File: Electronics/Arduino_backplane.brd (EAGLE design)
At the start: 100 x 80 mm, 40 parts, among them IC1 4013N, IC2 MCP4802, IC3 MCP4802, Q1 BF199, Q5 BF199, X1 M25-HD-20, X2 M25-HD-20

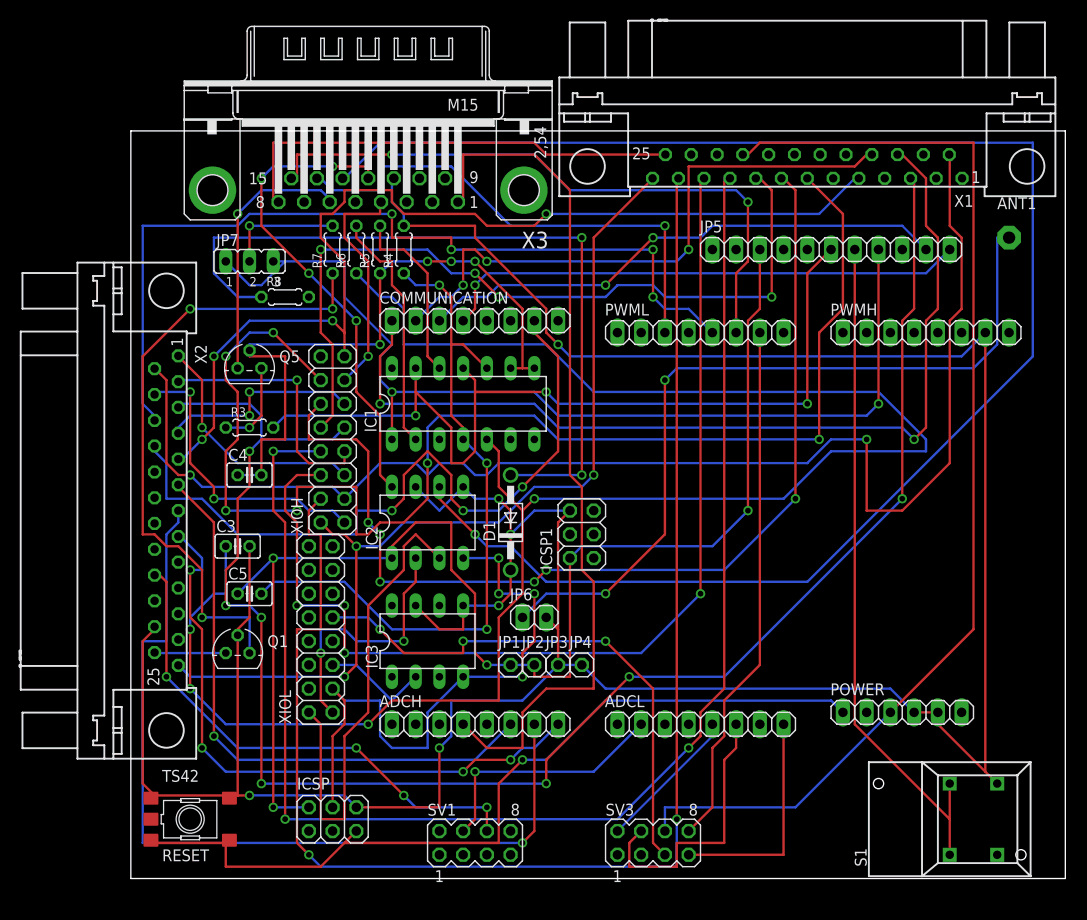
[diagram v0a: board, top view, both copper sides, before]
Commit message: Board layout improved, closer to Arduino pins. Signals renamed.
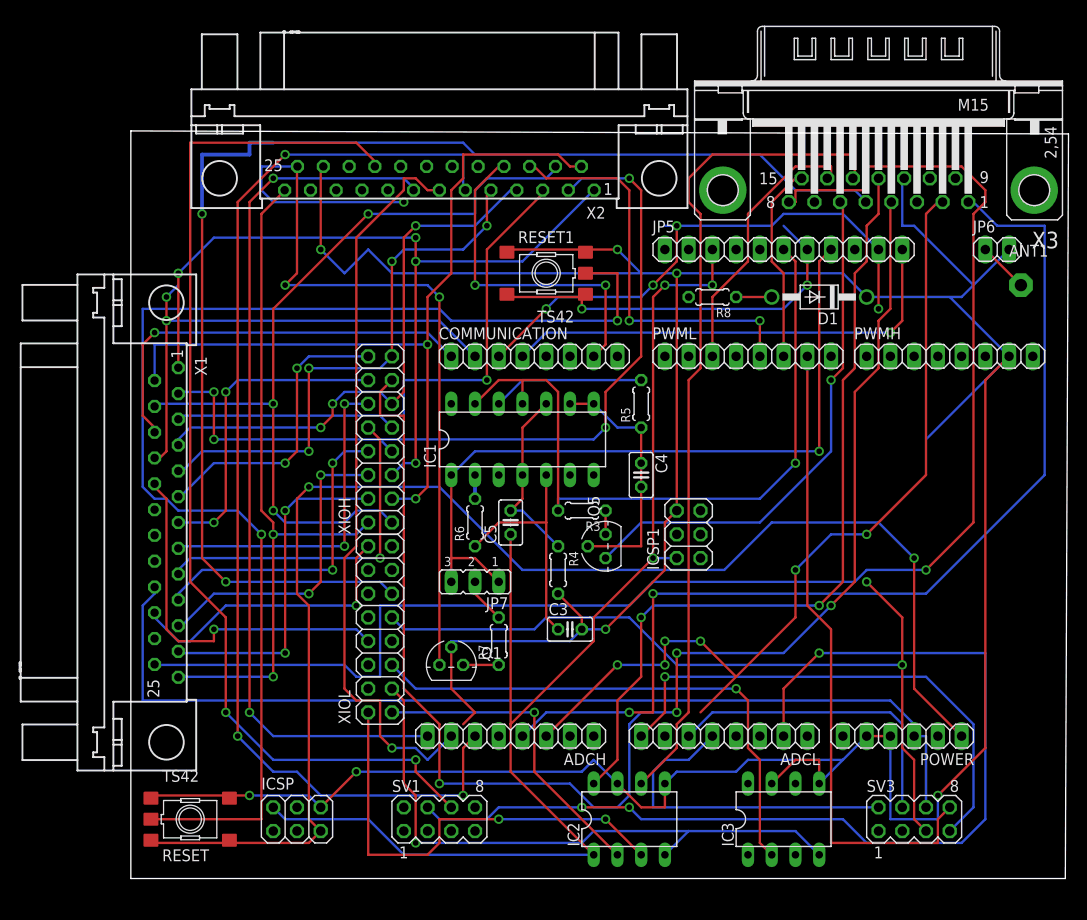
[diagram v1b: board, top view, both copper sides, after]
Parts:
- removed JP1, JP2, JP3, JP4: (no value), pinhead:1X01
- removed S1: 5501, switch:5501
- added RESET1: TS42, st-mod v1.4:TS42
- moved X1 78.5 mm to (3.81, 38.1), turned to 270 degrees
- moved JP6 63.3 mm to (92.7, 67.3)
- moved X3 54.6 mm to (80.0, 73.7)
- moved X2 46.0 mm to (33.0, 74.9), turned to 180 degrees
- moved R8 45.7 mm to (62.2, 62.2), turned to 180 degrees
- moved R7 45.5 mm to (39.4, 25.4)
- moved IC3 42.6 mm to (69.8, 6.35)
- moved Q5 42.6 mm to (50.8, 35.6), turned to 90 degrees
- moved JP7 41.9 mm to (36.8, 31.8), turned to 180 degrees
- moved C4 41.9 mm to (54.6, 43.2), turned to 270 degrees
- moved D1 40.9 mm to (73.7, 62.2), turned to 180 degrees
- moved IC2 38.4 mm to (53.3, 6.35)
- moved R4 38.1 mm to (45.7, 33.0), turned to 270 degrees
- moved C3 36.7 mm to (47.0, 26.7)
- moved R3 36.7 mm to (48.3, 39.4), turned to 180 degrees
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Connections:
- net INT0 renamed D2INT0
- net INT1 renamed D3INT1
- net INT2 renamed D18INT2
- net INT3 renamed D19INT3
- net INT4 renamed D20INT4
- net INT5 renamed D21INT5
- net N$1 renamed D25
- net N$10 renamed DACC
- net N$12 renamed D48
- net N$15 renamed WLES
- net N$19 renamed FUEL
- net N$2 renamed D4
- net N$20 renamed WLX
- net N$23 renamed VCC
- net N$3 renamed DACA
- net N$4 renamed D5
- net N$5 renamed D52
- net N$6 renamed DACB
- net N$8 renamed 5V
- net N$9 renamed A7
- net PA0 renamed D22
- net PA1 renamed D23
- net PA2 renamed D24
- net PA4 renamed D26
- net PA5 renamed D27
- net PA6 renamed D28
- net PA7 renamed D29
- net PB0 renamed D53
- net PB4 renamed D10
- net PB5 renamed D11
- net PB6 renamed D12
- net PB7 renamed D13
- net PC0 renamed D37
- net PC1 renamed D36
- net PC2 renamed D35
- net PC3 renamed D34
- net PC4 renamed D33
- net PC5 renamed D32
- net PC6 renamed D31
- net PC7 renamed D30
- net PD7 renamed D38
- net PG0 renamed D41
- net PG1 renamed D40
- net PG2 renamed D39
- net PH5 renamed D8
- net PH6 renamed D9
- net PL0 renamed D49
- net PL2 renamed D47
- net PL3 renamed D46
- net PL4 renamed D45
- net PL5 renamed D44
- net PL7 renamed D42
- net RXD2 renamed D17RXD2
- net RXD3 renamed D15RXD3
- net TXD2 renamed D16TXD2
- net TXD3 renamed D14TXD3
- removed net N$13: X3.5
- removed net N$37: R8.2
- removed net PL6: XIOL.11
- new net D43: X3.5, XIOL.11
- new net D51: IC2.4, IC3.4, XIOL.3
- new net DACD: IC3.6
- net +5V: no longer JP1.1, JP2.1
- net 5-GND: now also RESET1.5
- net GND: now also RESET1.3, RESET1.4; no longer JP3.1, JP4.1, S1.NO
- net N$28: now also RESET1.1, RESET1.2; no longer S1.1A, S1.1B
- net PB2: no longer IC2.4, IC3.4, XIOL.3
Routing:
- net N$35: track 201.4 -> 25.7 mm, vias 4 -> 0
- net D43: track 0.00 -> 140.2 mm, vias 0 -> 2
- net 5-GND: track 0.00 -> 136.4 mm, vias 0 -> 2
- net D25: track 25.1 -> 153.8 mm, vias 1 -> 4
- net D30: track 154.5 -> 34.0 mm, vias 3 -> 2
- net D34: track 156.7 -> 36.3 mm
- net D29: track 181.1 -> 62.3 mm, vias 7 -> 1
- net FUEL: track 49.4 -> 161.5 mm, vias 0 -> 1
- net D24: track 143.3 -> 34.1 mm, vias 6 -> 2
- net A10: track 0.00 -> 95.5 mm, vias 0 -> 6
- net DACB: track 176.7 -> 89.5 mm, vias 1 -> 0
- net WLX: track 7.67 -> 91.8 mm, vias 0 -> 3
- net A1: track 26.8 -> 109.4 mm, vias 1 -> 3
- net N$26: track 85.3 -> 5.39 mm, vias 2 -> 0
- net D32: track 113.3 -> 34.2 mm, vias 4 -> 2
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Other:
- board size 100 x 80 mm -> 100.3 x 80 mm

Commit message: Moved components for better routing; corrected connection errors.
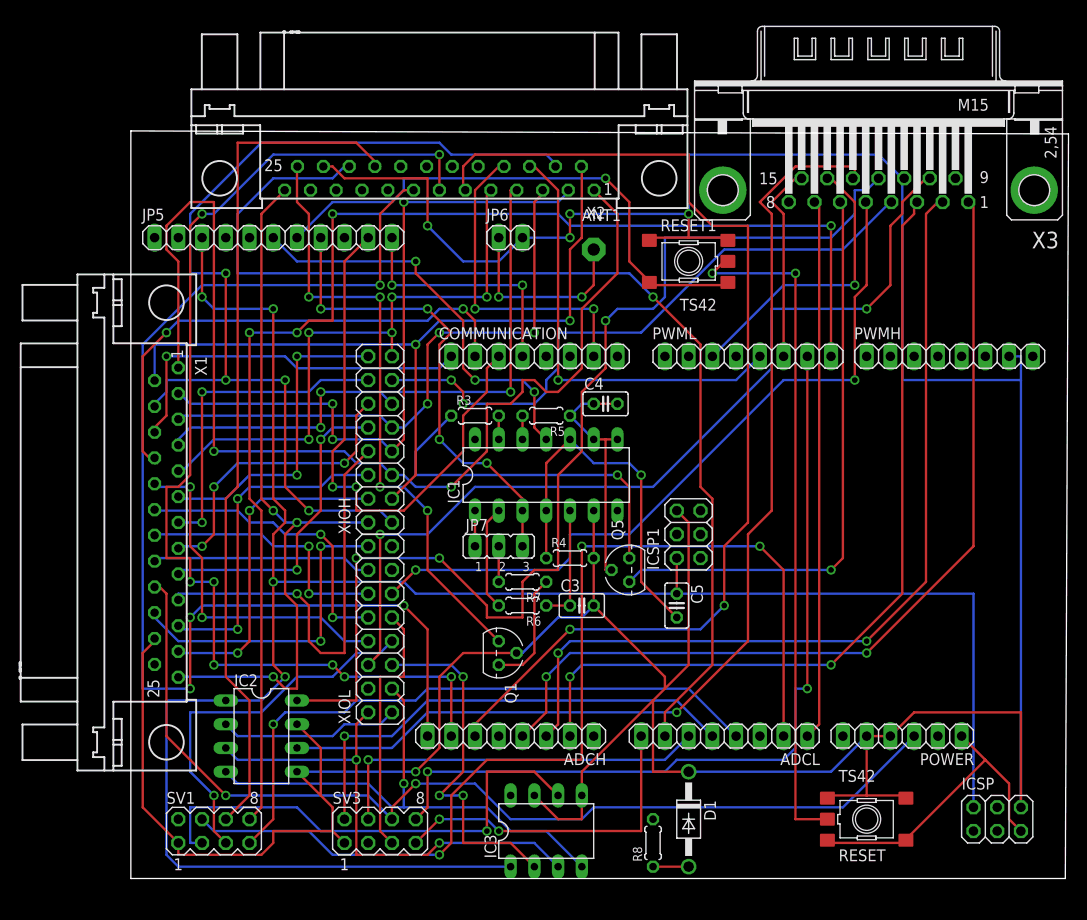
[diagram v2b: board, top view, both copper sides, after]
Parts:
- moved ICSP 74.9 mm to (92.7, 6.35)
- moved RESET 72.4 mm to (78.7, 6.35)
- moved R8 58.8 mm to (55.9, 3.81), turned to 90 degrees
- moved D1 57.6 mm to (59.7, 6.35), turned to 270 degrees
- moved SV3 57.2 mm to (26.7, 5.08)
- moved JP5 54.6 mm to (15.2, 68.6)
- moved JP6 52.1 mm to (40.6, 68.6)
- moved ANT1 45.9 mm to (49.5, 67.3)
- moved IC2 40.4 mm to (14.0, 15.2), turned to 270 degrees
- moved IC3 25.4 mm to (44.5, 5.08)
- moved SV1 24.2 mm to (8.89, 5.08)
- moved C5 19.9 mm to (58.4, 29.2), turned to 270 degrees
- moved R3 15.3 mm to (36.8, 49.5), turned to 0 degrees
- moved RESET1 15.3 mm to (59.7, 66.0)
- moved R6 10.2 mm to (41.9, 29.2), turned to 180 degrees
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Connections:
- net 5V renamed 5VBRK
- net A8 renamed N$2
- removed net A2: ADCL.3
- new net A6: ADCL.7, X2.23
- new net N$1: SV1.2
- new net N$3: XIOL.4
- new net N$4: IC1.1, JP7.1
- new net N$5: IC1.13, R3.2
- net +5V: now also IC3.1
- net A0: now also ADCL.1
- net A3: now also SV1.7
- net A9: now also ADCH.2
- net D40: now also X1.21
- net D42: now also X1.20
- net D44: now also X1.19
- net D47: now also SV1.5
- net D48: now also XIOL.6
- net D52: now also IC3.3
- net D7: now also SV1.8
- net DACD: now also SV1.3
- net GND: now also IC1.6, SV1.1, SV3.1, X1.24
- net N$25: no longer IC1.13, R3.2
- net N$30: now also IC1.3; no longer IC1.1, JP7.1
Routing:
- net FUEL: track 161.5 -> 0.00 mm, vias 1 -> 0
- net D7: track 0.00 -> 141.8 mm, vias 0 -> 4
- net A6: track 0.00 -> 117.6 mm, vias 0 -> 1
- net RESET: track 151.0 -> 34.0 mm, vias 2 -> 0
- net D48: track 0.00 -> 97.3 mm, vias 0 -> 2
- net A9: track 0.00 -> 88.3 mm, vias 0 -> 2
- net D25: track 153.8 -> 67.2 mm, vias 4 -> 2
- net +5V: track 139.6 -> 225.2 mm, vias 3 -> 4
- net A3: track 0.00 -> 67.0 mm, vias 0 -> 1
- net 5-GND: track 136.4 -> 73.3 mm
- net D43: track 140.2 -> 80.2 mm
- net D45: track 87.1 -> 27.7 mm, vias 2 -> 0
- net A0: track 0.00 -> 58.2 mm
- net DACD: track 0.00 -> 52.9 mm, vias 0 -> 1
- net A14: track 79.4 -> 119.8 mm, vias 1 -> 8
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
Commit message: Corrected some overlaps
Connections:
- removed net N$3: XIOL.4
- net D14TXD3: now also X2.18
- net D16TXD2: now also X2.20
- net D17RXD2: now also X2.19
- net D3INT1: now also X2.21
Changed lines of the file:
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@@
 <signal name="D3INT1">
 <contactref element="PWML" pad="4"/>
+<contactref element="X2" pad="21"/>
+<wire x1="28.8798" y1="76.2" x2="64.77" y2="55.88" width="0" layer="19" extent="1-1"/>
 </signal>
 <signal name="D2INT0">
@@
 <signal name="D17RXD2">
 <contactref element="COMMUNICATION" pad="5"/>
+<contactref element="X2" pad="19"/>
+<wire x1="44.45" y1="55.88" x2="34.3916" y2="76.2" width="0" layer="19" extent="1-1"/>
 </signal>
 <signal name="D15RXD3">
@@
 <signal name="D16TXD2">
 <contactref element="COMMUNICATION" pad="6"/>
+<contactref element="X2" pad="20"/>
+<wire x1="46.99" y1="55.88" x2="31.6484" y2="76.2" width="0" layer="19" extent="1-1"/>
 </signal>
 <signal name="D14TXD3">
 <contactref element="COMMUNICATION" pad="8"/>
+<contactref element="X2" pad="18"/>
+<wire x1="52.07" y1="55.88" x2="37.1602" y2="76.2" width="0" layer="19" extent="1-1"/>
 </signal>
 <signal name="D37">
@@
 <wire x1="27.94" y1="27.94" x2="29.21" y2="26.67" width="0.254" layer="1"/>
 </signal>
-<signal name="N$3">
-<contactref element="XIOL" pad="4"/>
-</signal>
 <signal name="FUEL">

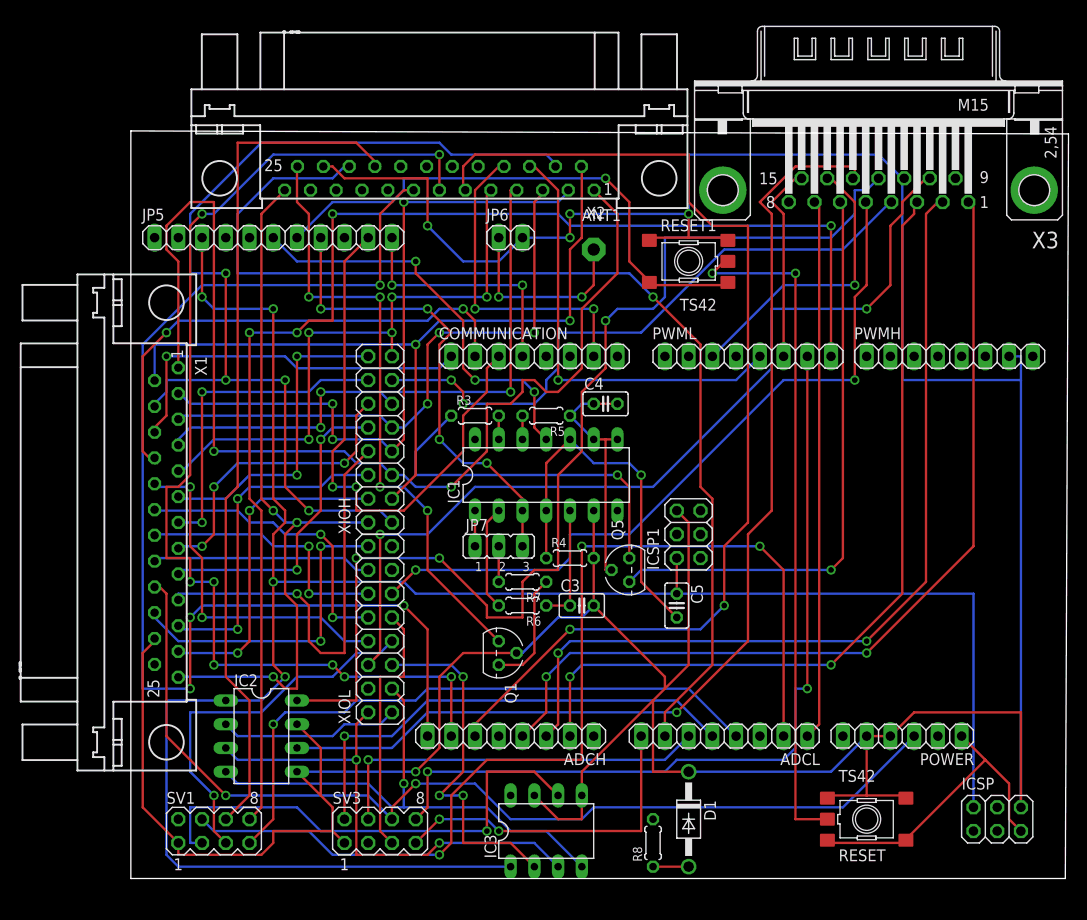
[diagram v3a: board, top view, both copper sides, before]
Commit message: Reduced warnings; 97% routed.
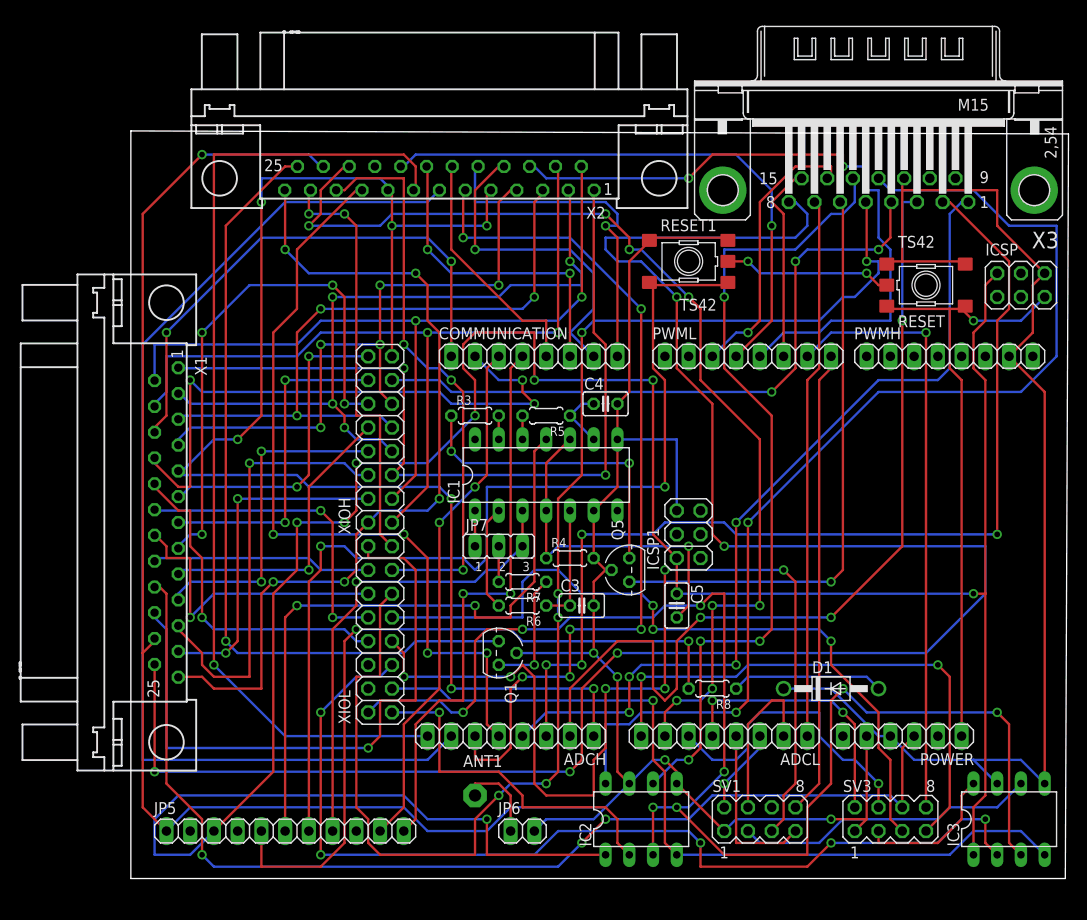
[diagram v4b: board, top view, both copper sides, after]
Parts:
- moved JP5 63.5 mm to (16.5, 5.08)
- moved JP6 63.5 mm to (41.9, 5.08)
- moved ANT1 59.8 mm to (36.8, 8.89)
- moved SV1 58.4 mm to (67.3, 6.35)
- moved RESET 57.5 mm to (85.1, 63.5)
- moved ICSP 57.2 mm to (95.2, 63.5)
- moved SV3 54.6 mm to (81.3, 6.35)
- moved IC3 49.5 mm to (94.0, 6.35)
- moved IC2 41.6 mm to (54.6, 6.35), turned to 0 degrees
- moved D1 20.7 mm to (74.9, 20.3), turned to 0 degrees
- moved R8 17.7 mm to (62.2, 20.3), turned to 180 degrees
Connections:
- removed net +3V3: POWER.2
- removed net AREF: PWMH.8
- removed net D10: PWMH.3
- removed net D11: PWMH.4
- removed net D12: PWMH.5
- removed net D13: PWMH.6
- removed net D8: PWMH.1
- removed net D9: PWMH.2
- removed net N$11: C4.1, C4.2, IC1.8, IC1.9, Q5.2, R5.1
- new net N$3: JP5.5, R8.2
- net A12: now also X2.10
- net D23: now also ADCH.1, X2.9
- net D39: now also X2.12
- net D41: now also X2.11
- net DACC: now also SV3.3
- net GND: now also C4.2, IC1.8, JP5.1, Q5.2
- net N$1: now also ADCL.3
- net N$2: now also C4.1, IC1.9, R5.1; no longer ADCH.1
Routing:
- net FUEL: track 0.00 -> 211.4 mm, vias 0 -> 5
- net D52: track 53.4 -> 150.7 mm, vias 2 -> 8
- net D48: track 97.3 -> 0.00 mm, vias 2 -> 0
- net A1: track 112.7 -> 17.6 mm, vias 3 -> 0
- net D7: track 141.8 -> 49.8 mm, vias 4 -> 0
- net 5VBRK: track 91.9 -> 0.00 mm
- net D23: track 64.7 -> 155.8 mm, vias 5 -> 7
- net A12: track 0.00 -> 84.6 mm, vias 0 -> 4
- net N$3: track 0.00 -> 78.3 mm, vias 0 -> 2
- net D47: track 40.3 -> 110.9 mm, vias 1 -> 6
- net D49: track 38.2 -> 106.6 mm, vias 3 -> 5
- net D43: track 80.2 -> 148.4 mm, vias 2 -> 6
- net D3INT1: track 0.00 -> 61.2 mm, vias 0 -> 1
- net D41: track 0.00 -> 61.1 mm, vias 0 -> 3
- net +5V: track 225.2 -> 284.2 mm, vias 4 -> 8
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
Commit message: Arduino pins placed correctly; 100% routed. SOme errors.
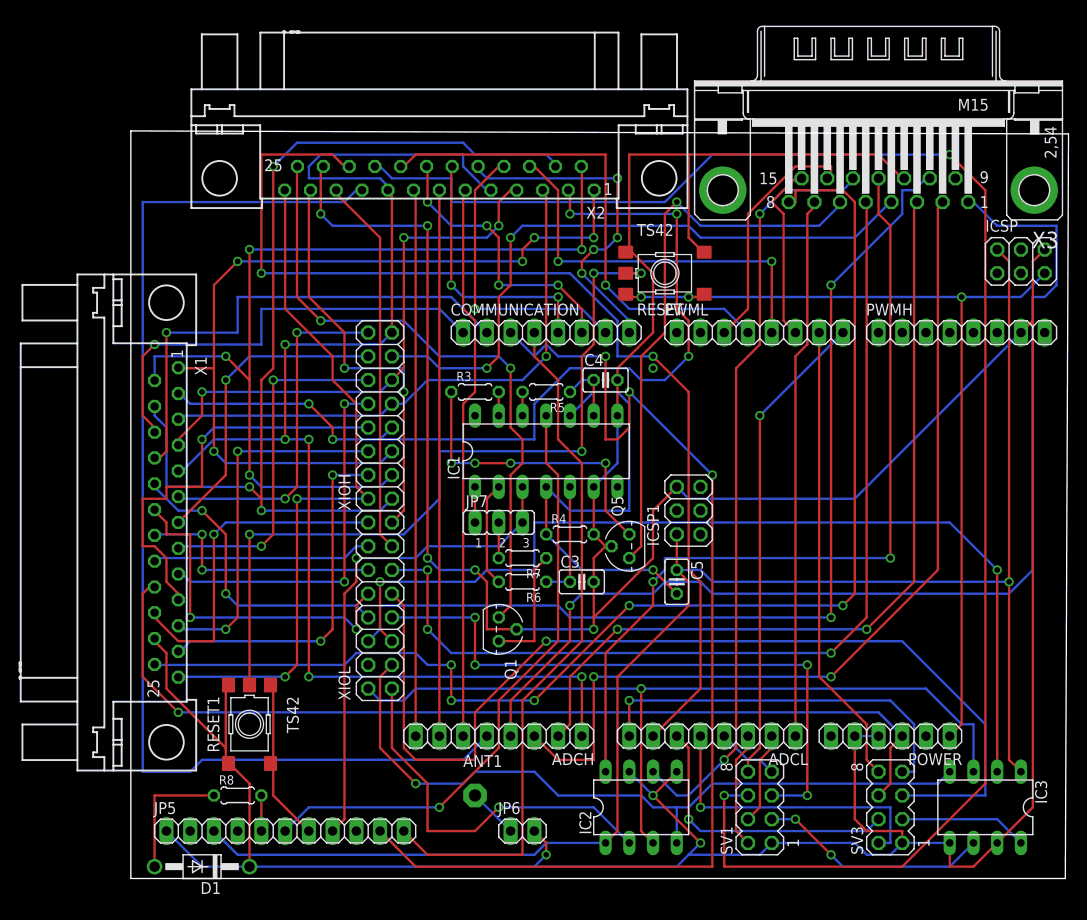
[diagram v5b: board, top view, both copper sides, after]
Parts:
- moved D1 70.0 mm to (7.62, 1.27), turned to 180 degrees
- moved RESET1 68.3 mm to (12.7, 16.5), turned to 270 degrees
- moved R8 52.1 mm to (11.4, 8.89), turned to 0 degrees
- moved RESET 28.0 mm to (57.1, 64.8)
- moved IC3 2.84 mm to (91.4, 7.62), turned to 180 degrees
- moved PWMH 2.84 mm to (88.9, 58.4)
- moved COMMUNICATION 2.84 mm to (44.5, 58.4)
- moved PWML 2.84 mm to (67.3, 58.4)
- moved C4 2.54 mm to (50.8, 53.3)
- moved ICSP 2.54 mm to (95.2, 66.0)
- moved Q1 2.54 mm to (39.4, 26.7)
- moved C3 2.54 mm to (48.3, 31.8)
- moved C5 2.54 mm to (58.4, 31.8)
- moved IC1 2.54 mm to (44.5, 45.7)
- moved ICSP1 2.54 mm to (59.7, 39.4)
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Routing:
- net 5VBRK: track 0.00 -> 177.4 mm, vias 0 -> 2
- net +5V: track 284.2 -> 173.7 mm, vias 8 -> 1
- net D48: track 0.00 -> 105.5 mm, vias 0 -> 2
- net N$28: track 107.7 -> 17.8 mm, vias 2 -> 0
- net FUEL: track 211.4 -> 135.3 mm
- net N$3: track 78.3 -> 3.81 mm, vias 2 -> 0
- net 5-GND: track 18.8 -> 85.0 mm, vias 2 -> 4
- net D19INT3: track 56.1 -> 119.7 mm, vias 2 -> 3
- net D52: track 150.7 -> 89.5 mm, vias 8 -> 1
- net A14: track 117.1 -> 58.4 mm
- net GND: track 424.4 -> 476.3 mm, vias 5 -> 8
- net A15: track 105.5 -> 58.6 mm, vias 1 -> 0
- net D43: track 148.4 -> 104.3 mm, vias 6 -> 3
- net D47: track 110.9 -> 67.3 mm, vias 6 -> 4
- net A12: track 84.6 -> 123.4 mm, vias 4 -> 0
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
